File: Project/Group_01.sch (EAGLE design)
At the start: 29 parts, among them J1 POWER_JACKPTH_LOCK, U1 +12v, U4 TMUX1208

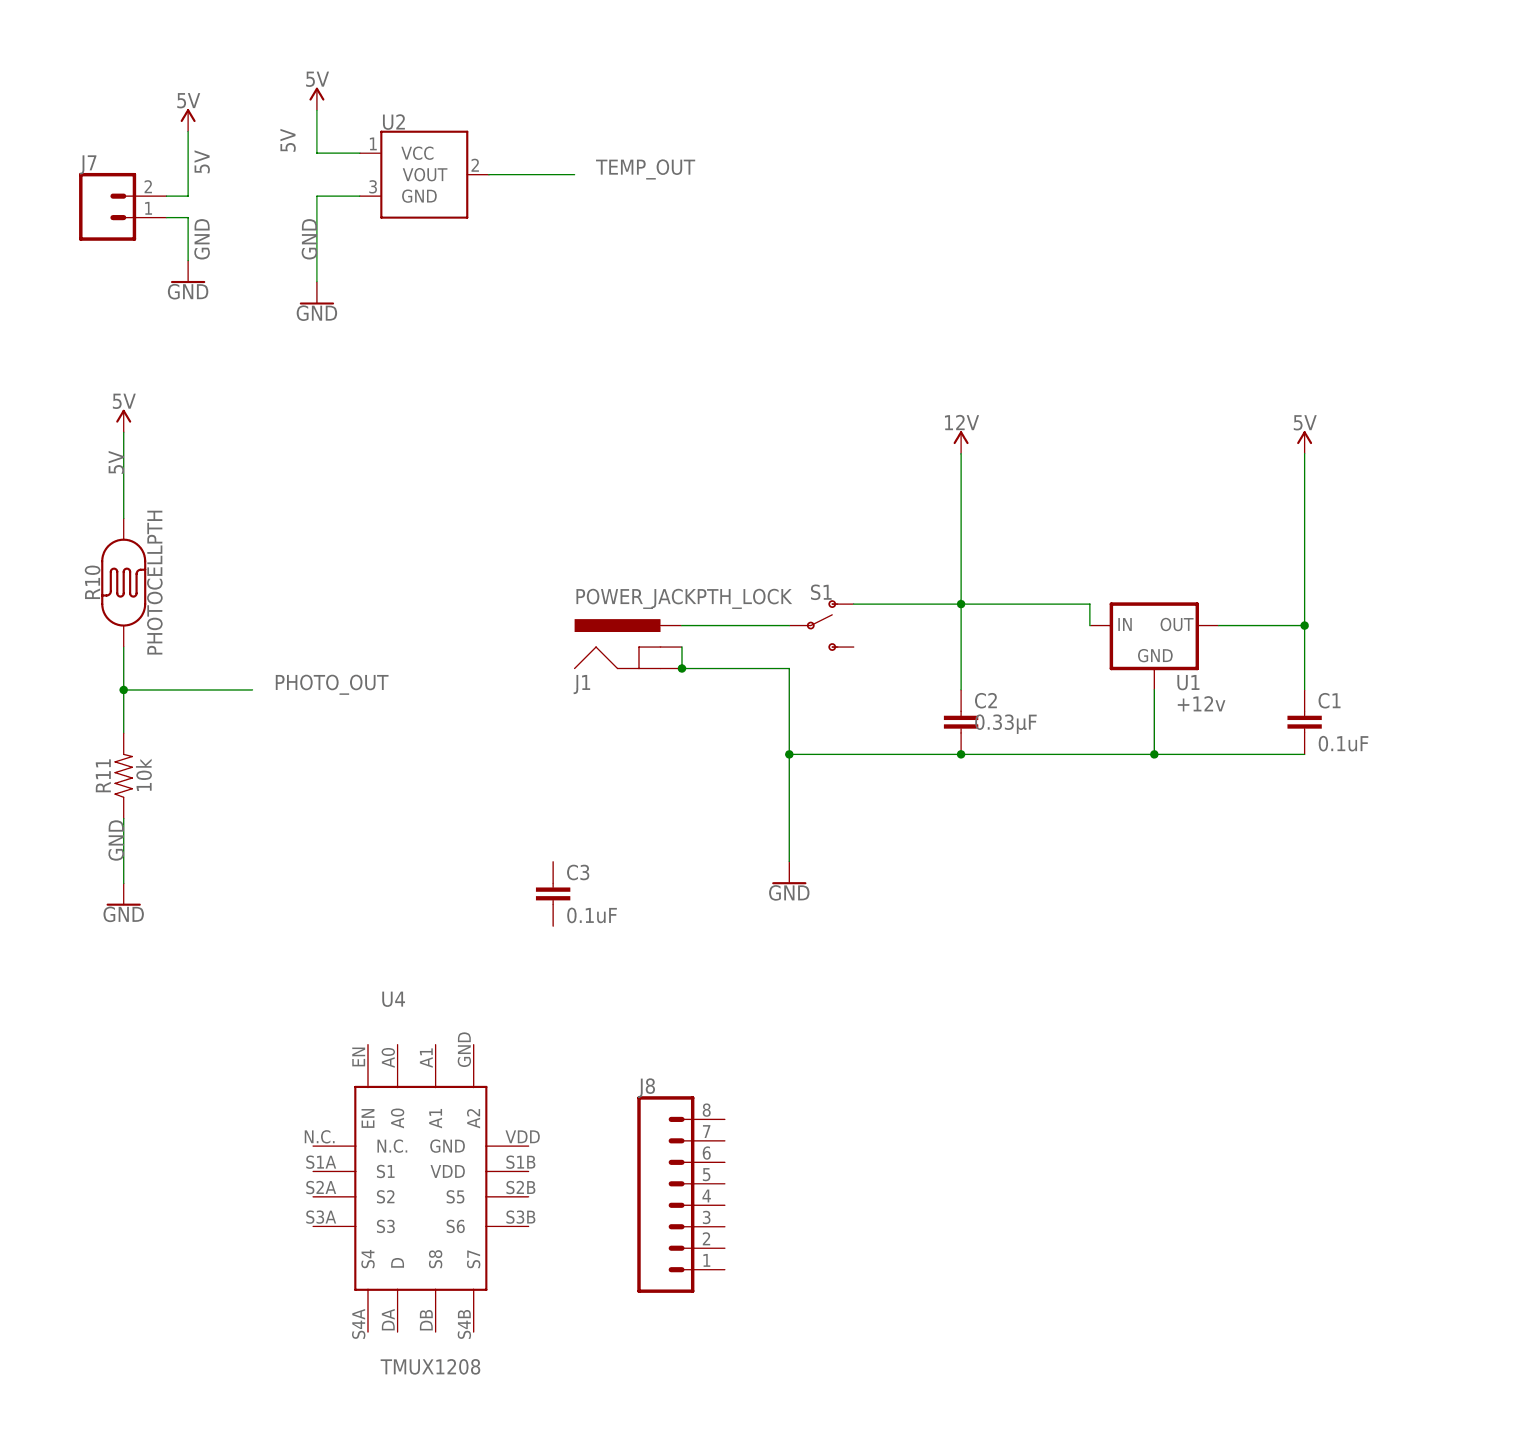
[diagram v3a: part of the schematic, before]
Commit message: Changed QFN16 and finished schematics
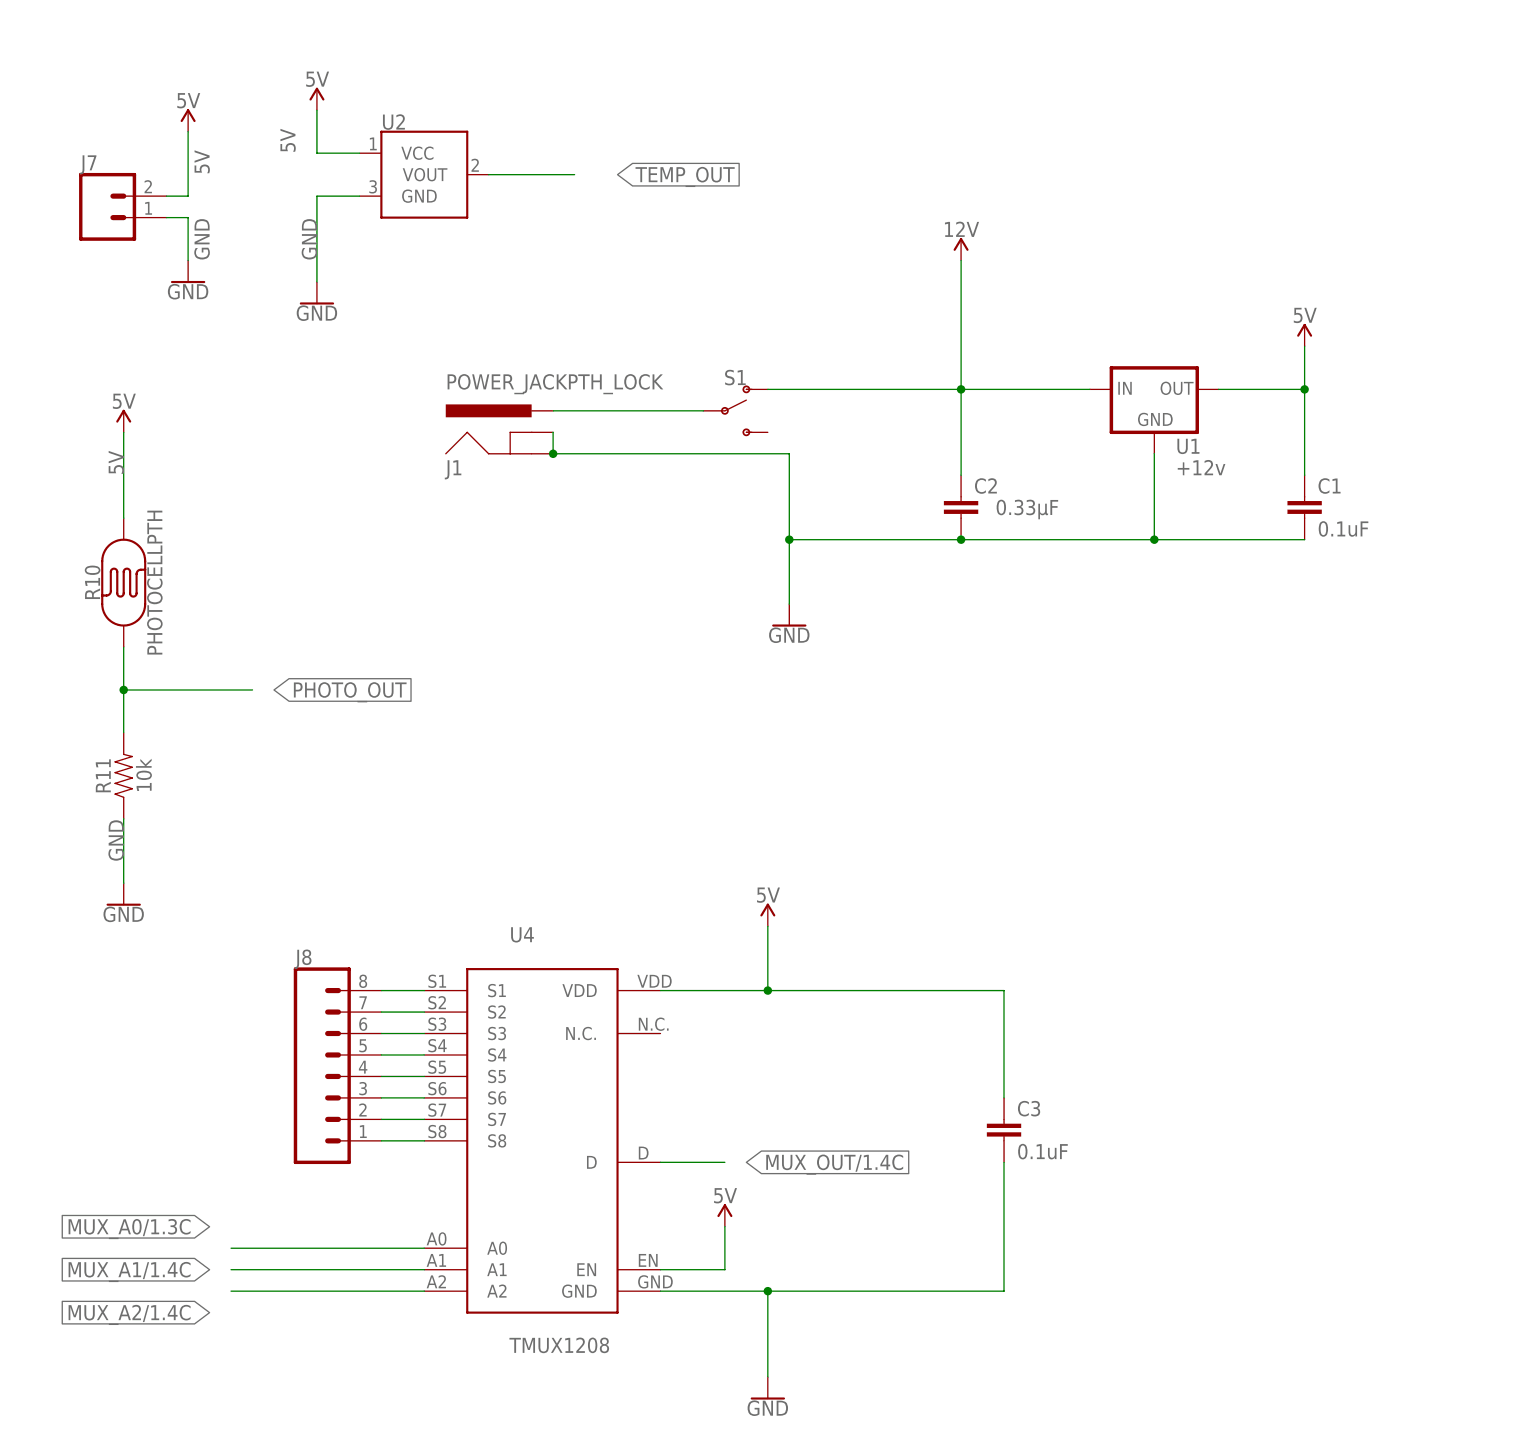
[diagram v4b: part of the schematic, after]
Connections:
- new net MUX_A0/1.3C: U4.A0
- new net MUX_A1/1.4C: U4.A1
- new net MUX_A2/1.4C: U4.A2
- new net MUX_OUT/1.4C: U4.D
- new net N$10: J8.8, U4.S1
- new net N$11: J8.7, U4.S2
- new net N$12: J8.6, U4.S3
- new net N$13: J8.5, U4.S4
- new net N$14: J8.4, U4.S5
- new net N$15: J8.3, U4.S6
- new net N$16: J8.2, U4.S7
- new net N$17: J8.1, U4.S8
- net 5V: now also C3.1, U4.EN, U4.VDD
- net GND: now also C3.2, U4.GND
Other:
- moved on the sheet: C1, C2, C3, J1, J8, S1, U1, U4

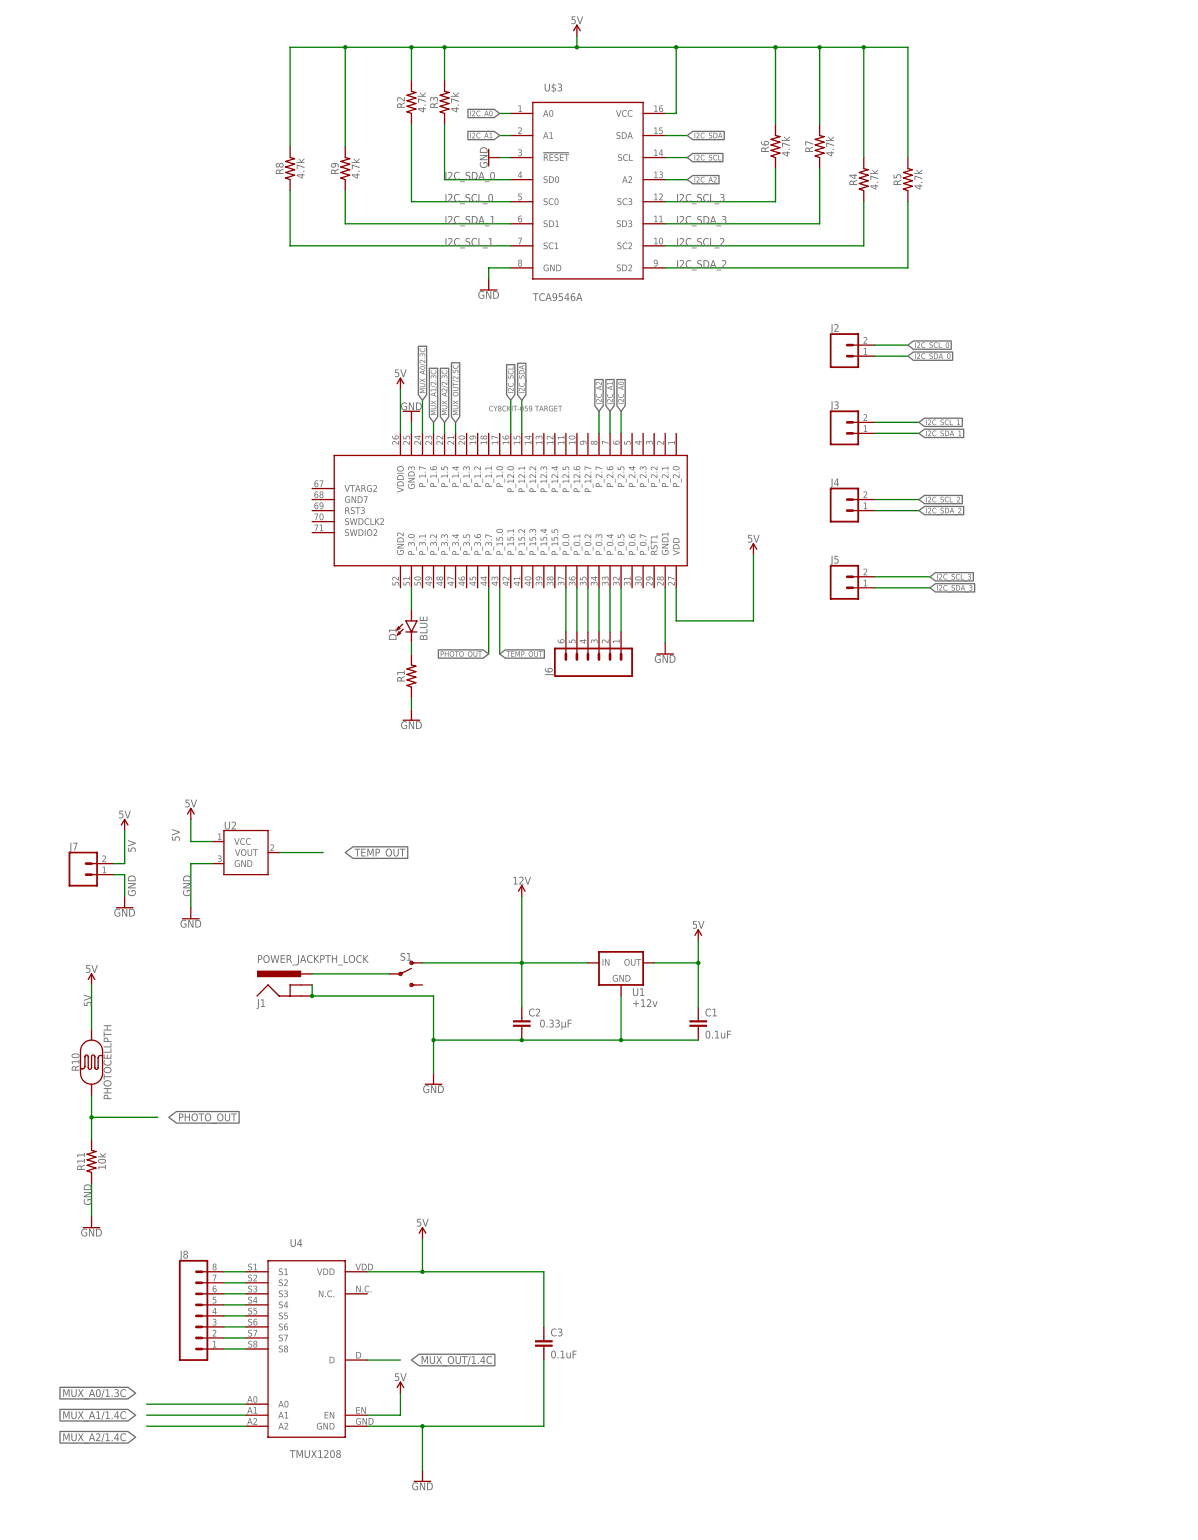
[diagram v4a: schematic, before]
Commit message: Added comments on schematic, board layout, dru file
The board still needs to be routed
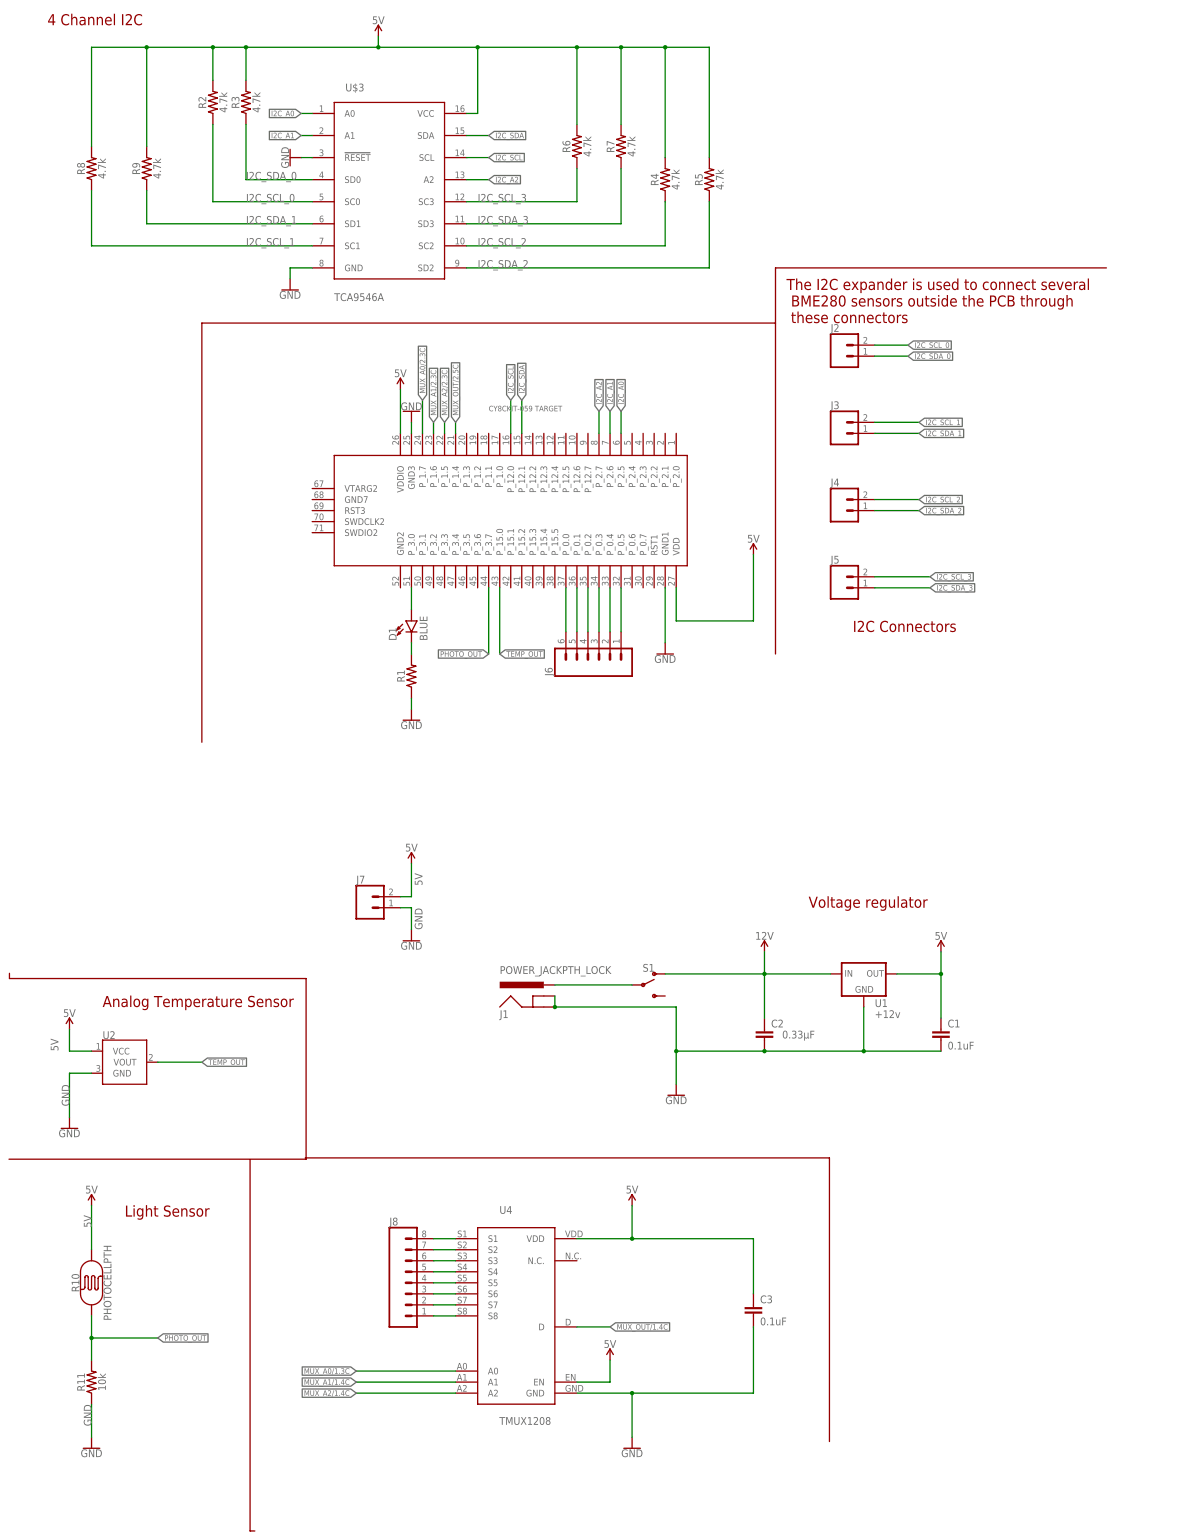
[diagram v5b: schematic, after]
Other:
- note added: "4 Channel I2C"
- note added: "Analog Temperature Sensor"
- note added: "I2C Connectors"
- note added: "Light Sensor"
- note added: "The I2C expander is used to connect several BME280 sensors outside the PCB through these connectors"
- note added: "Voltage regulator"
- moved on the sheet: C1, C2, C3, J1, J7, J8, R10, R11, R2, R3, R4, R5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

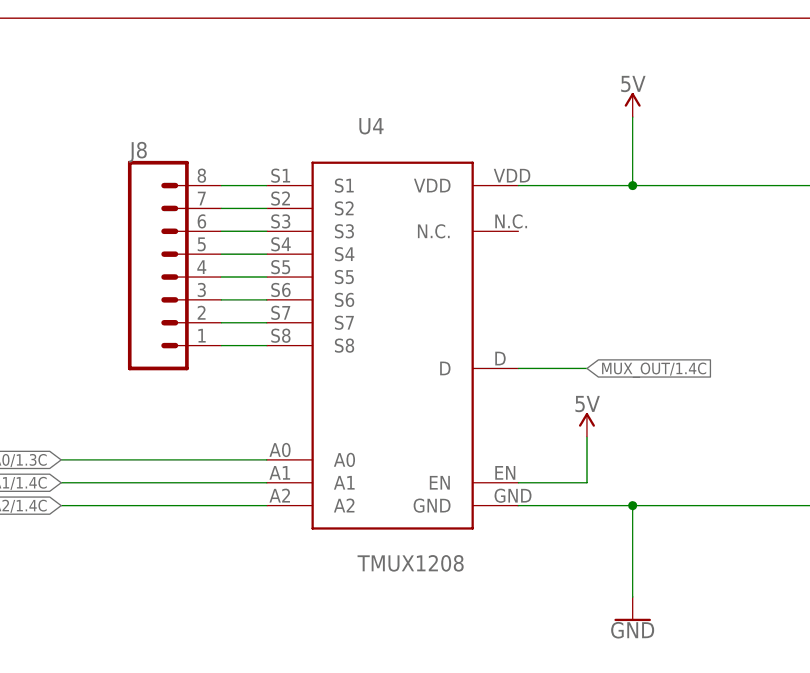
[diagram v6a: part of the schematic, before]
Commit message: Silkscreen improved
It's the tname layer
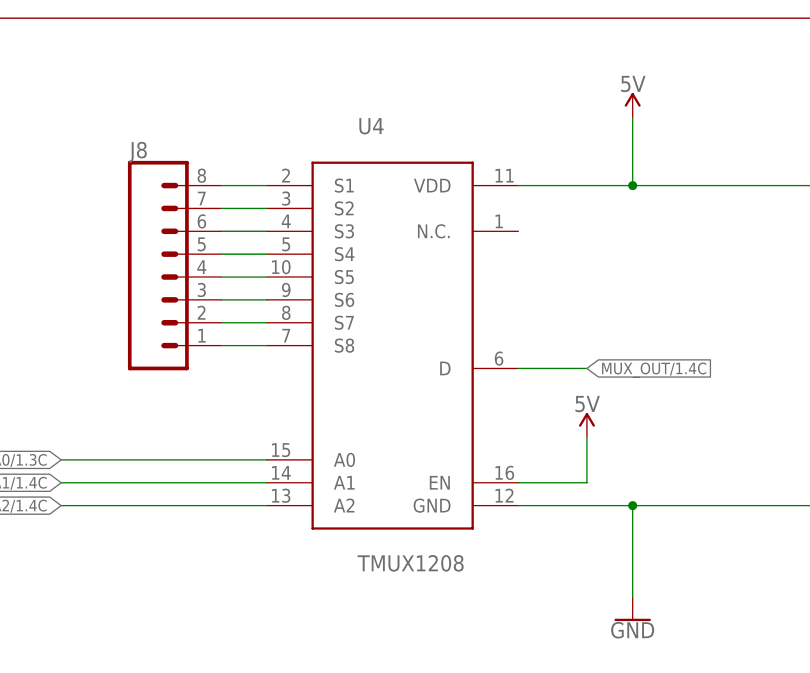
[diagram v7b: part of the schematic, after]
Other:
- moved on the sheet: U4
